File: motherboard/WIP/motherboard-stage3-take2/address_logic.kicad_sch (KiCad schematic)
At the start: 13 parts, among them U23 GAL 22V10, U24 74LS670, U25 74LS670, U26 GAL 22V10, U27 GAL16V8, U28 74HC245

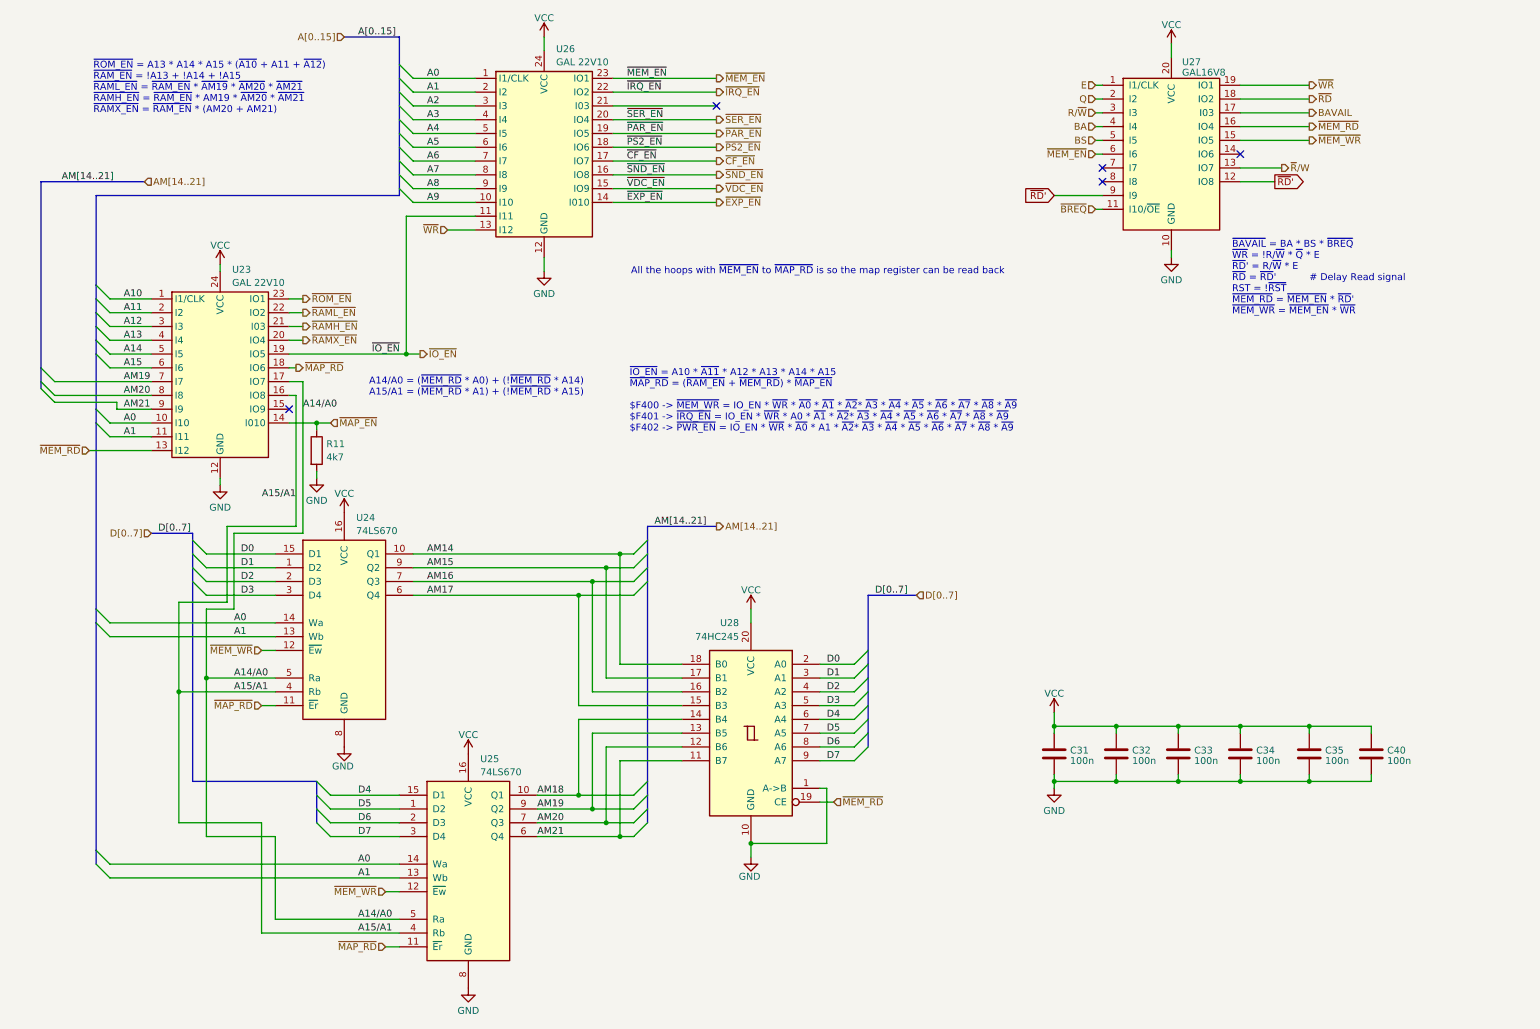
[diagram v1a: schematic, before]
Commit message: Updated stage 2 and stage 3, and started on a cf addon
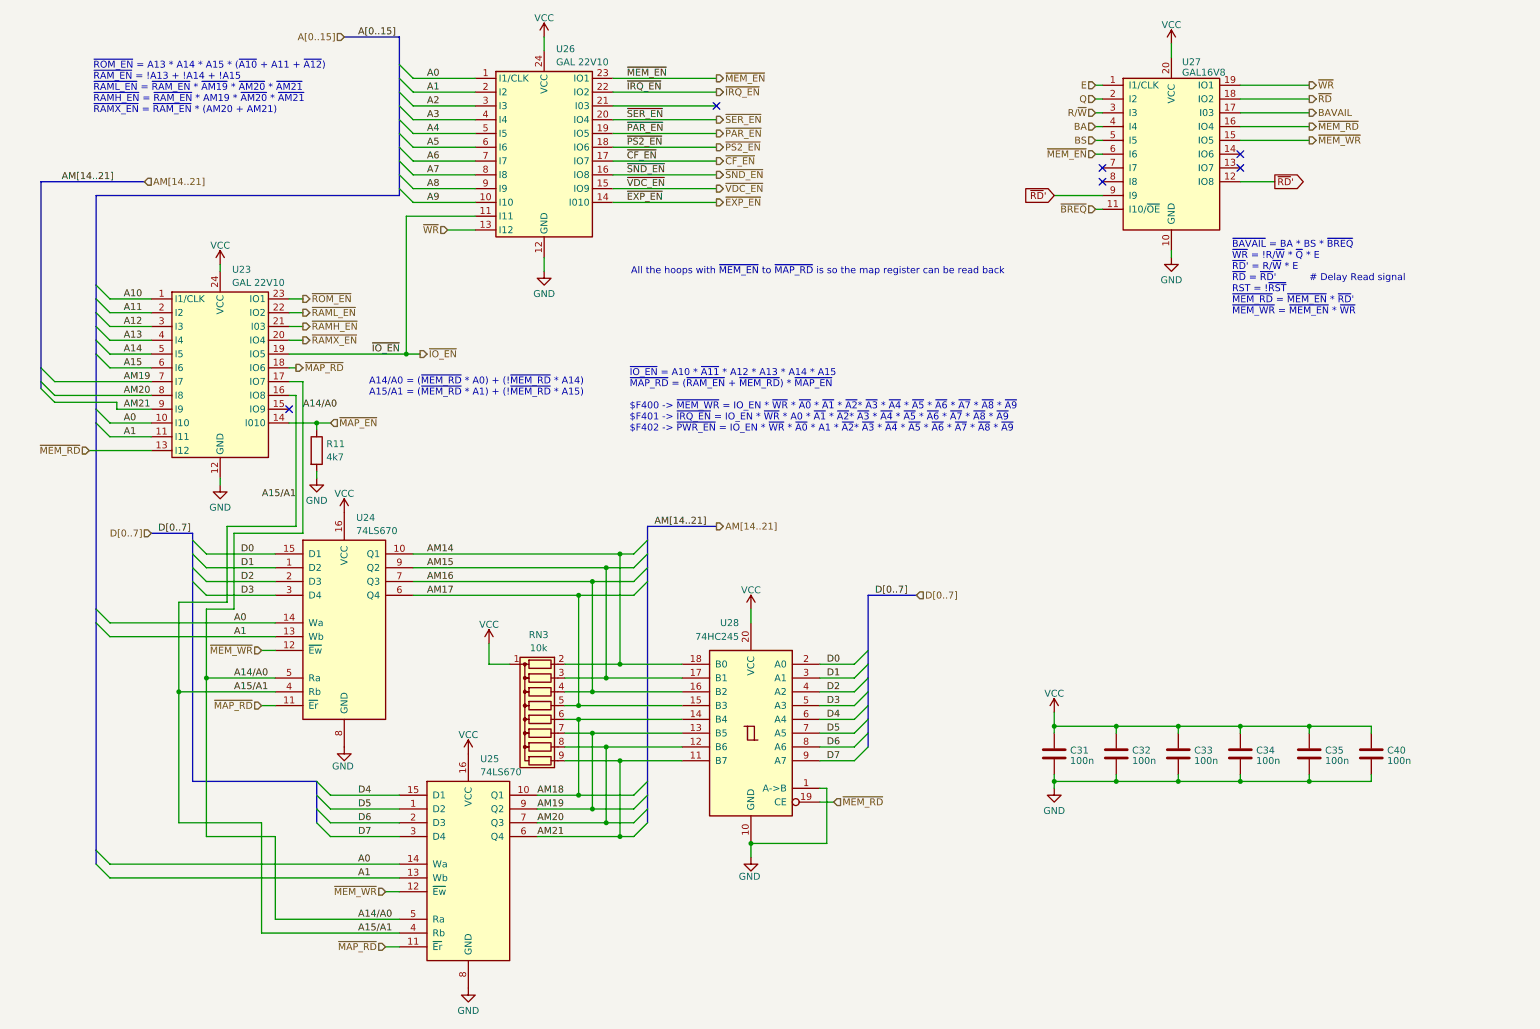
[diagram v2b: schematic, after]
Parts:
- added RN3: 10k, Resistor_THT:R_Array_SIP9, symbol Device:R_Network08
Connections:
- net AM14: now also RN3.2 (R1)
- net AM15: now also RN3.3 (R2)
- net AM16: now also RN3.4 (R3)
- net AM17: now also RN3.5 (R4)
- net AM18: now also RN3.6 (R5)
- net AM19: now also RN3.7 (R6)
- net AM20: now also RN3.8 (R7)
- net AM21: now also RN3.9 (R8)
- net VCC: now also RN3.1 (common)
- net ~{R}/W: no longer names the net of U27.13 (IO7)
- no-connect marks 5 -> 6
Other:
- company: (none) -> Eric Lind
- title: (none) -> MicroLind - Logic, address & signal

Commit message: Updates to a lot!
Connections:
- net GND: now also RN3.1 (common)
- net VCC: no longer RN3.1 (common)
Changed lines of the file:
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@@
 	(wire
 		(pts
-			(xy 106.68 129.54) (xy 106.68 133.35)
+			(xy 106.68 133.35) (xy 106.68 137.16)
 		)
 		(stroke
@@
 	)
 	(symbol
-		(lib_id "power:VCC")
-		(at 106.68 129.54 0)
-		(unit 1)
-		(exclude_from_sim no)
-		(in_bom yes)
-		(on_board yes)
-		(dnp no)
-		(fields_autoplaced yes)
-		(property "Reference" "#PWR032"
-			(at 106.68 133.35 0)
-			(effects
-				(font
-					(size 1.27 1.27)
-				)
-				(hide yes)
-			)
-		)
-		(property "Value" "VCC"
-			(at 106.68 126.0381 0)
-			(effects
-				(font
-					(size 1.27 1.27)
-				)
-			)
-		)
-		(property "Footprint" ""
-			(at 106.68 129.54 0)
-			(effects
-				(font
-					(size 1.27 1.27)
-				)
-				(hide yes)
-			)
-		)
-		(property "Datasheet" ""
-			(at 106.68 129.54 0)
-			(effects
-				(font
-					(size 1.27 1.27)
-				)
-				(hide yes)
-			)
-		)
-		(property "Description" ""
-			(at 106.68 129.54 0)
-			(effects
-				(font
-					(size 1.27 1.27)
-				)
-				(hide yes)
-			)
-		)
-		(pin "1"
-		)
-		(instances
-			(project "motherboard"
-				(path "/4cf1c087-5c32-4958-ab30-5e92afc4ef4b/3f2dac53-f913-4700-9643-6801a186951e"
-					(reference "#PWR032")
-					(unit 1)
-				)
-			)
-		)
-	)
-	(symbol
 		(lib_id "power:GND")
 		(at 102.87 193.04 0)
@@
 					(unit 1)
 				)
+			)
+		)
+	)
+	(symbol
+		(lib_id "power:GND")
+		(at 106.68 137.16 0)
+		(unit 1)
+		(exclude_from_sim no)
+		(in_bom yes)
+		(on_board yes)
+		(dnp no)
+		(property "Reference" "#PWR032"
+			(at 106.68 143.51 0)
+			(effects
+				(font
+					(size 1.27 1.27)
+				)
+				(hide yes)
+			)
+		)
+		(property "Value" "GND"
+			(at 106.426 140.716 0)
+			(effects
+				(font
+					(size 1.27 1.27)
+				)
+			)
+		)
+		(property "Footprint" ""
+			(at 106.68 137.16 0)
+			(effects
+				(font
+					(size 1.27 1.27)
+				)
+				(hide yes)
+			)
+		)
+		(property "Datasheet" ""
+			(at 106.68 137.16 0)
+			(effects
+				(font
+					(size 1.27 1.27)
+				)
+				(hide yes)
+			)
+		)
+		(property "Description" ""
+			(at 106.68 137.16 0)
+			(effects
+				(font
+					(size 1.27 1.27)
+				)
+				(hide yes)
+			)
+		)
+		(pin "1"
+		)
+		(instances
+			(project "motherboard"
+				(path "/4cf1c087-5c32-4958-ab30-5e92afc4ef4b/3f2dac53-f913-4700-9643-6801a186951e"
+					(reference "#PWR032")
+					(unit 1)
+				)

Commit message: Updated stage 3
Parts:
- added R18, R19, R20: 10k, Resistor_THT:R_Axial_DIN0204_L3.6mm_D1.6mm_P7.62mm_Horizontal, symbol Device:R
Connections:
- net BA: now also R18.2
- net BS: now also R19.2
- net R/~{W}: now also R20.1
- net VCC: now also R18.1, R19.1, R20.2
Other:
- note added: "Address Logic"
- note added: "Memory Logic"
- note added: "Signal Logic"
